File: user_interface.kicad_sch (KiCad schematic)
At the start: 26 parts, among them J1201 PH1-08-UA, J1202 EMI shield frame, J1203 FH12A-40S-0.5SH(55), U1201 TCA9554PW, U1202 AP5725FDCG-7, X1201 Keypad 3x4, X1202 NHD-4.3-480272EF-ASXP

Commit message: Refactor text with ChatGPT and make schematics more readable
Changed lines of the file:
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@@
 		)
 	)
-	(text_box "The graphical interface is a TFT LCD with a backlight.\n\nTouchscreen functionality is provided via the I2C interface.\nThe pins can be disconnected if a non-touchscreen TFT LCD is used."
+	(text_box "The graphical interface consists of a TFT LCD with backlighting.\n- Touchscreen functionality: Provided via the I²C interface.\n- Optional configuration: The I²C pins can be disconnected if a non-touchscreen TFT LCD is used."
 		(exclude_from_sim no)
 		(at 210.82 63.5 0)
@@
 		)
 	)
-	(text_box "They keypad interface is for a 3/4x4 matrix membrane keypad.\n\nThe keypad buttons are polled continuously and button presses are detected by switching rows and columns HIGH/LOW and changing states between INPUT/OUTPUT.\n\nThe keypad buttons and their usage is application defined and thus not hard-set."
+	(text_box "The keypad interface supports a 3×4 or 4×4 matrix membrane keypad.\n- Button scanning: Key presses are detected by continuously polling the keypad and toggling rows and columns between HIGH/LOW and INPUT/OUTPUT states.\n- Application-defined mapping: The functionality and usage of individual keypad buttons are defined by the application and are not fixed."
 		(exclude_from_sim no)
 		(at 13.97 63.5 0)

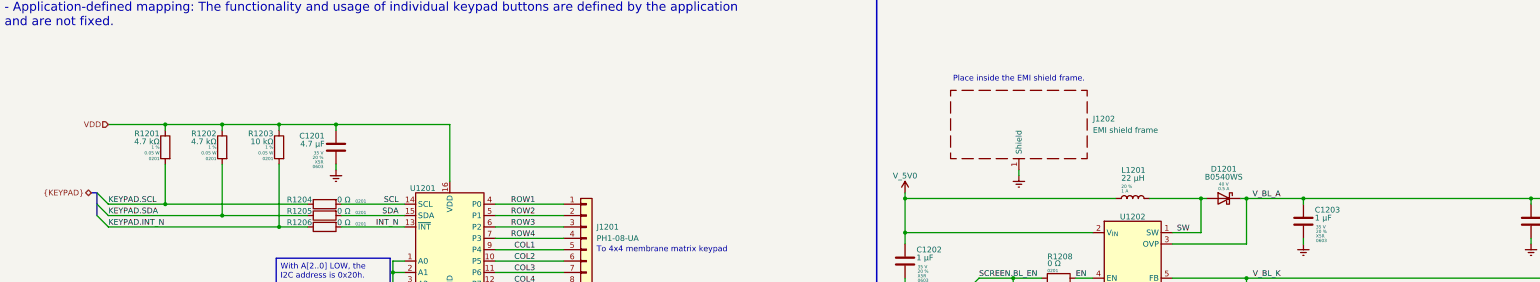
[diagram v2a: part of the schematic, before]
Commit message: Fix power connections
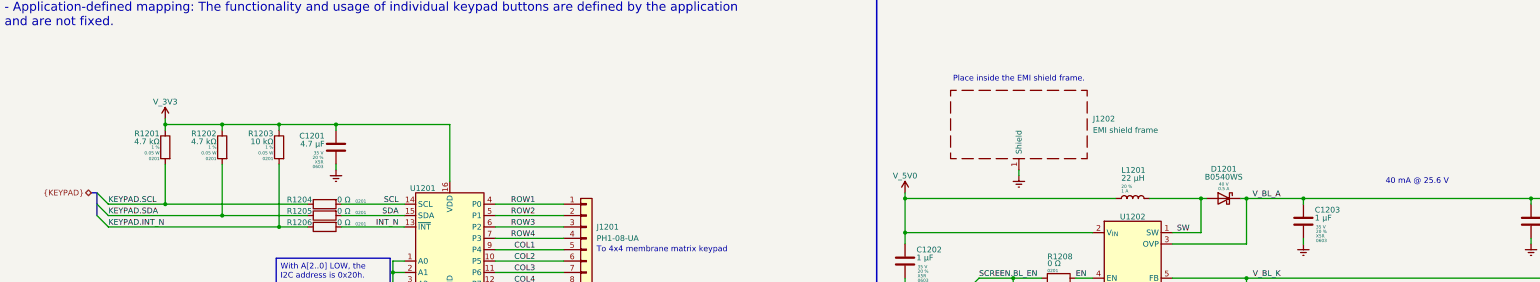
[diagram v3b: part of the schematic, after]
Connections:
- net VDD is gone; now on net V_3V3: C1201.1, R1201.1, R1202.1, R1203.1, U1201.16 (VDD)
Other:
- note added: "40 mA @ 25.6 V"
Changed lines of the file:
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@@
 		)
 	)
+	(text "40 mA @ 25.6 V"
+		(exclude_from_sim no)
+		(at 330.2 114.3 0)
+		(effects
+			(font
+				(size 1.27 1.27)
+			)
+		)
+	)
 	(text "Notes"
 		(exclude_from_sim no)
@@
 	)
 	(junction
-		(at 328.93 143.51)
-		(diameter 0)
-		(color 0 0 0 0)
-	)
-	(junction
 		(at 354.33 227.33)
 		(diameter 0)
@@
 	)
 	(junction
-		(at 50.8 101.6)
-		(diameter 0)
-		(color 0 0 0 0)
-	)
-	(junction
 		(at 354.33 246.38)
 		(diameter 0)
@@
 	)
 	(junction
+		(at 50.8 101.6)
+		(diameter 0)
+		(color 0 0 0 0)
+	)
+	(junction
 		(at 114.3 143.51)
 		(diameter 0)
@@
 	)
 	(junction
+		(at 328.93 143.51)
+		(diameter 0)
+		(color 0 0 0 0)
+	)
+	(junction
 		(at 304.8 118.11)
 		(diameter 0)
@@
 	(wire
 		(pts
-			(xy 38.1 101.6) (xy 50.8 101.6)
+			(xy 90.17 124.46) (xy 104.14 124.46)
 		)
 		(stroke
@@
 		)
 	)
-	(wire
+	(bus
 		(pts
-			(xy 90.17 124.46) (xy 104.14 124.46)
+			(xy 311.15 173.99) (xy 311.15 176.53)
 		)
 		(stroke
@@
 	(bus
 		(pts
-			(xy 311.15 173.99) (xy 311.15 176.53)
+			(xy 311.15 217.17) (xy 311.15 224.79)
 		)
 		(stroke
@@
 		)
 	)
-	(bus
+	(wire
 		(pts
-			(xy 311.15 217.17) (xy 311.15 224.79)
+			(xy 281.94 118.11) (xy 283.21 118.11)
 		)
 		(stroke
@@
 	(wire
 		(pts
-			(xy 281.94 118.11) (xy 283.21 118.11)
+			(xy 365.76 246.38) (xy 368.3 246.38)
 		)
 		(stroke
@@
 	(wire
 		(pts
-			(xy 365.76 246.38) (xy 368.3 246.38)
+			(xy 50.8 100.33) (xy 50.8 101.6)
 		)
 		(stroke
@@
 	(wire
 		(pts
+			(xy 328.93 142.24) (xy 328.93 143.51)
+		)
+		(stroke
+			(width 0)
+			(type default)
+		)
+	)
+	(wire
+		(pts
 			(xy 292.1 135.89) (xy 292.1 144.78)
 		)
@@
 		)
 	)
-	(wire
-		(pts
-			(xy 328.93 142.24) (xy 328.93 143.51)
-		)
-		(stroke
-			(width 0)
-			(type default)
-		)
-	)
 	(bus
 		(pts
@@
 		)
 	)
-	(hierarchical_label "VDD"
-		(shape input)
-		(at 38.1 101.6 180)
-		(effects
-			(font
-				(size 1.27 1.27)
-			)
-			(justify right)
-		)
-	)
 	(hierarchical_label "{SCREEN}"
 		(shape bidirectional)
@@
 		(dnp no)
 		(fields_autoplaced yes)
-		(property "Reference" "#PWR01209"
+		(property "Reference" "#PWR01210"
 			(at 374.65 254 0)
 			(effects
@@
 			(project "linux-sbc"
 				(path "/fa11a02f-8043-4153-ab69-88d766503017/530a7454-1232-4a53-8117-19eb81379b71"
-					(reference "#PWR01209")
+					(reference "#PWR01210")
 					(unit 1)
 				)
@@
 		(dnp no)
 		(fields_autoplaced yes)
-		(property "Reference" "#PWR01201"
+		(property "Reference" "#PWR01202"
 			(at 88.9 118.11 0)
 			(effects
@@
 			(project "linux-sbc"
 				(path "/fa11a02f-8043-4153-ab69-88d766503017/530a7454-1232-4a53-8117-19eb81379b71"
-					(reference "#PWR01201")
+					(reference "#PWR01202")
 					(unit 1)
 				)
@@
 		(dnp no)
 		(fields_autoplaced yes)
-		(property "Reference" "#PWR01202"
+		(property "Reference" "#PWR01203"
 			(at 114.3 151.13 0)
 			(effects
@@
 			(project "linux-sbc"
 				(path "/fa11a02f-8043-4153-ab69-88d766503017/530a7454-1232-4a53-8117-19eb81379b71"
-					(reference "#PWR01202")
+					(reference "#PWR01203")
 					(unit 1)
 				)
@@
 		(on_board yes)
 		(dnp no)
-		(property "Reference" "#PWR01203"
+		(property "Reference" "#PWR01204"
 			(at 215.9 120.65 0)
 			(effects
@@
 			(project "linux-sbc"
 				(path "/fa11a02f-8043-4153-ab69-88d766503017/530a7454-1232-4a53-8117-19eb81379b71"
-					(reference "#PWR01203")
+					(reference "#PWR01204")
 					(unit 1)
 				)
@@
 		(dnp no)
 		(fields_autoplaced yes)
-		(property "Reference" "#PWR01204"
+		(property "Reference" "#PWR01205"
 			(at 215.9 161.29 0)
 			(effects
@@
 			(project "linux-sbc"
 				(path "/fa11a02f-8043-4153-ab69-88d766503017/530a7454-1232-4a53-8117-19eb81379b71"
-					(reference "#PWR01204")
+					(reference "#PWR01205")
 					(unit 1)
 				)
@@
 		(dnp no)
 		(fields_autoplaced yes)
-		(property "Reference" "#PWR01206"
+		(property "Reference" "#PWR01207"
 			(at 304.8 134.62 0)
 			(effects
@@
 			(project "linux-sbc"
 				(path "/fa11a02f-8043-4153-ab69-88d766503017/530a7454-1232-4a53-8117-19eb81379b71"
-					(reference "#PWR01206")
+					(reference "#PWR01207")
 					(unit 1)
 				)
@@
 		(dnp no)
 		(fields_autoplaced yes)
-		(property "Reference" "#PWR01205"
+		(property "Reference" "#PWR01206"
 			(at 241.3 119.38 0)
 			(effects
@@
 			(project "linux-sbc"
 				(path "/fa11a02f-8043-4153-ab69-88d766503017/530a7454-1232-4a53-8117-19eb81379b71"
-					(reference "#PWR01205")
+					(reference "#PWR01206")
 					(unit 1)
 				)
@@
 		(dnp no)
 		(fields_autoplaced yes)
-		(property "Reference" "#PWR01208"
+		(property "Reference" "#PWR01209"
 			(at 355.6 134.62 0)
 			(effects
@@
 			(project "linux-sbc"
 				(path "/fa11a02f-8043-4153-ab69-88d766503017/530a7454-1232-4a53-8117-19eb81379b71"
-					(reference "#PWR01208")
+					(reference "#PWR01209")
 					(unit 1)
 				)
@@
 	)
 	(symbol
+		(lib_id "power:VCC")
+		(at 328.93 142.24 0)
+		(unit 1)
+		(exclude_from_sim no)
+		(in_bom yes)
+		(on_board yes)
+		(dnp no)
+		(property "Reference" "#PWR01208"
+			(at 328.93 146.05 0)
+			(effects
+				(font
+					(size 1.27 1.27)
+				)
+				(hide yes)
+			)
+		)
+		(property "Value" "V_3V3"
+			(at 328.93 139.192 0)
+			(effects
+				(font
+					(size 1.27 1.27)
+				)
+				(justify bottom)
+			)
+		)
+		(property "Footprint" ""
+			(at 328.93 142.24 0)
+			(effects
+				(font
+					(size 1.27 1.27)
+				)
+				(hide yes)
+			)
+		)
+		(property "Datasheet" ""
+			(at 328.93 142.24 0)
+			(effects
+				(font
+					(size 1.27 1.27)
+				)
+				(hide yes)
+			)
+		)
+		(property "Description" "Power symbol creates a global label with name \"VCC\""
+			(at 328.93 142.24 0)
+			(effects
+				(font
+					(size 1.27 1.27)
+				)
+				(hide yes)
+			)
+		)
+		(pin "1"
+		)
+		(instances
+			(project "linux-sbc"
+				(path "/fa11a02f-8043-4153-ab69-88d766503017/530a7454-1232-4a53-8117-19eb81379b71"
+					(reference "#PWR01208")
+					(unit 1)
+				)
+			)
+		)
+	)
+	(symbol
 		(lib_id "Device:C")
 		(at 328.93 240.03 0)
@@
 	)
 	(symbol
-		(lib_id "power:VCC")
-		(at 328.93 142.24 0)
-		(unit 1)
-		(exclude_from_sim no)
-		(in_bom yes)
-		(on_board yes)
-		(dnp no)
-		(property "Reference" "#PWR01207"
-			(at 328.93 146.05 0)
-			(effects
-				(font
-					(size 1.27 1.27)
-				)
-				(hide yes)
-			)
-		)
-		(property "Value" "V_3V3"
-			(at 328.93 139.192 0)
-			(effects
-				(font
-					(size 1.27 1.27)
-				)
-				(justify bottom)
-			)
-		)
-		(property "Footprint" ""
-			(at 328.93 142.24 0)
-			(effects
-				(font
-					(size 1.27 1.27)
-				)
-				(hide yes)
-			)
-		)
-		(property "Datasheet" ""
-			(at 328.93 142.24 0)
-			(effects
-				(font
-					(size 1.27 1.27)
-				)
-				(hide yes)
-			)
-		)
-		(property "Description" "Power symbol creates a global label with name \"VCC\""
-			(at 328.93 142.24 0)
-			(effects
-				(font
-					(size 1.27 1.27)
-				)
-				(hide yes)
-			)
-		)
-		(pin "1"
-		)
-		(instances
-			(project "linux-sbc"
-				(path "/fa11a02f-8043-4153-ab69-88d766503017/530a7454-1232-4a53-8117-19eb81379b71"
-					(reference "#PWR01207")
-					(unit 1)
-				)
-			)
-		)
-	)
-	(symbol
 		(lib_id "Device:R")
 		(at 63.5 106.68 0)
@@
 					(unit 1)
 				)
+			)
+		)
+	)
+	(symbol
+		(lib_id "power:VCC")
+		(at 50.8 100.33 0)
+		(unit 1)
+		(exclude_from_sim no)
+		(in_bom yes)
+		(on_board yes)
+		(dnp no)
+		(property "Reference" "#PWR01201"
+			(at 50.8 104.14 0)
+			(effects
+				(font
+					(size 1.27 1.27)
+				)
+				(hide yes)
+			)
+		)
+		(property "Value" "V_3V3"
+			(at 50.8 97.282 0)
+			(effects
+				(font
+					(size 1.27 1.27)
+				)
+				(justify bottom)
+			)
+		)
+		(property "Footprint" ""
+			(at 50.8 100.33 0)
+			(effects
+				(font
+					(size 1.27 1.27)
+				)
+				(hide yes)
+			)
+		)
+		(property "Datasheet" ""
+			(at 50.8 100.33 0)
+			(effects
+				(font
+					(size 1.27 1.27)
+				)
+				(hide yes)
+			)
+		)
+		(property "Description" "Power symbol creates a global label with name \"VCC\""
+			(at 50.8 100.33 0)
+			(effects
+				(font
+					(size 1.27 1.27)
+				)
+				(hide yes)
+			)
+		)
+		(pin "1"
+		)
+		(instances
+			(project "linux-sbc"
+				(path "/fa11a02f-8043-4153-ab69-88d766503017/530a7454-1232-4a53-8117-19eb81379b71"
+					(reference "#PWR01201")
+					(unit 1)
+				)

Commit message: Clean up schematics
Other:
- note removed: "To 4x4 membrane matrix keypad"
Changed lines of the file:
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@@
 	(title_block
 		(title "Linux SBC")
-		(date "2025-12-19")
+		(date "2025-12-26")
 		(rev "v1.0.0")
 	)
@@
 		)
 	)
-	(text "To 4x4 membrane matrix keypad"
-		(exclude_from_sim no)
-		(at 147.066 129.5401 0)
-		(effects
-			(font
-				(size 1.27 1.27)
-			)
-			(justify left)
-		)
-	)
 	(text "Place inside the EMI shield frame."
 		(exclude_from_sim no)
@@
 	)
 	(junction
-		(at 101.6 134.62)
-		(diameter 0)
-		(color 0 0 0 0)
-	)
-	(junction
 		(at 368.3 224.79)
 		(diameter 0)
@@
 	)
 	(junction
-		(at 101.6 137.16)
-		(diameter 0)
-		(color 0 0 0 0)
-	)
-	(junction
 		(at 215.9 125.73)
 		(diameter 0)
@@
 	)
 	(junction
+		(at 102.87 134.62)
+		(diameter 0)
+		(color 0 0 0 0)
+	)
+	(junction
 		(at 215.9 118.11)
 		(diameter 0)
@@
 	)
 	(junction
+		(at 102.87 137.16)
+		(diameter 0)
+		(color 0 0 0 0)
+	)
+	(junction
 		(at 240.03 153.67)
 		(diameter 0)
@@
 	(wire
 		(pts
-			(xy 104.14 132.08) (xy 101.6 132.08)
+			(xy 102.87 132.08) (xy 104.14 132.08)
 		)
 		(stroke
@@
 	(wire
 		(pts
+			(xy 102.87 134.62) (xy 104.14 134.62)
+		)
+		(stroke
+			(width 0)
+			(type default)
+		)
+	)
+	(wire
+		(pts
 			(xy 88.9 101.6) (xy 88.9 102.87)
 		)
@@
 	(wire
 		(pts
-			(xy 101.6 137.16) (xy 101.6 143.51)
+			(xy 102.87 137.16) (xy 102.87 143.51)
 		)
 		(stroke
@@
 	(wire
 		(pts
+			(xy 102.87 137.16) (xy 104.14 137.16)
+		)
+		(stroke
+			(width 0)
+			(type default)
+		)
+	)
+	(wire
+		(pts
 			(xy 304.8 118.11) (xy 355.6 118.11)
 		)
@@
 	(wire
 		(pts
-			(xy 101.6 132.08) (xy 101.6 134.62)
+			(xy 102.87 132.08) (xy 102.87 134.62)
 		)
 		(stroke
@@
 	(wire
 		(pts
-			(xy 101.6 134.62) (xy 101.6 137.16)
+			(xy 102.87 134.62) (xy 102.87 137.16)
 		)
 		(stroke
@@
 	(wire
 		(pts
-			(xy 114.3 143.51) (xy 101.6 143.51)
+			(xy 114.3 143.51) (xy 102.87 143.51)
 		)
 		(stroke
@@
 	(wire
 		(pts
-			(xy 101.6 134.62) (xy 104.14 134.62)
-		)
-		(stroke
-			(width 0)
-			(type default)
-		)
-	)
-	(wire
-		(pts
 			(xy 313.69 199.39) (xy 369.57 199.39)
 		)
@@
 	(wire
 		(pts
-			(xy 101.6 137.16) (xy 104.14 137.16)
-		)
-		(stroke
-			(width 0)
-			(type default)
-		)
-	)
-	(wire
-		(pts
 			(xy 275.59 143.51) (xy 276.86 143.51)
 		)
@@
 		(dnp no)
 		(property "Reference" "J1201"
-			(at 147.066 124.46 0)
+			(at 147.32 125.73 0)
 			(effects
 				(font
@@
 		)
 		(property "Value" "PH1-08-UA"
-			(at 147.066 127 0)
+			(at 147.32 128.27 0)
 			(effects
 				(font
@@
 		(on_board yes)
 		(dnp no)
-		(fields_autoplaced yes)
 		(property "Reference" "J1203"
-			(at 377.19 184.5055 0)
+			(at 377.19 182.88 0)
 			(effects
 				(font
@@
 		)
 		(property "Value" "FH12A-40S-0.5SH(55)"
-			(at 377.19 187.0455 0)
+			(at 377.19 185.42 0)
 			(effects
 				(font

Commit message: Layout the UI section
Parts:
- added R1210, R1211, R1212, R1213, R1214, R1215, R1216, R1217, R1218, R1219, R1220, R1221, R1222, R1223, R1224, R1225, R1226, R1227, R1228, R1229, R1230, R1231, R1232, R1233, R1234, R1235, R1236, R1237, R1238, R1239, R1240, R1241, R1242: 0 Ω, perfect_footprints:R_0201_0603Metric, symbol Device:R
- C1205: footprint Capacitor_SMD:C_0603_1608Metric -> perfect_footprints:C_0402_1005Metric; Digi-Key Part Number 490-7205-1-ND -> 1276-6836-1-ND; MPN GRM188R6YA475KE15D -> CL05A475MO5NUNC; Manufacturer Murata Electronics -> Samsung Electro-Mechanics; Size 0603 -> 0402; Voltage rating 35 V -> 16 V
- J1202: footprint RF_Shielding:Laird_Technologies_BMI-S-203-F_26.21x26.21mm -> RF_Shielding:Laird_Technologies_BMI-S-202-F_16.50x16.50mm
- renumbered R1208 to R1207, R1207 to R1208, R1210 to R1243, R1211 to R1244
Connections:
- net EN: now also R1208.1
- net SCL: now also J1203.39 (Pin_39), R1241.2
- net SCREEN.B0: now also R1226.1; no longer J1203.21 (Pin_21)
- net SCREEN.B1: now also R1227.1; no longer J1203.22 (Pin_22)
- net SCREEN.B2: now also R1228.1; no longer J1203.23 (Pin_23)
- net SCREEN.B3: now also R1229.1; no longer J1203.24 (Pin_24)
- net SCREEN.B4: now also R1230.1; no longer J1203.25 (Pin_25)
- net SCREEN.B5: now also R1231.1; no longer J1203.26 (Pin_26)
- net SCREEN.B6: now also R1232.1; no longer J1203.27 (Pin_27)
- net SCREEN.B7: now also R1233.1; no longer J1203.28 (Pin_28)
- net SCREEN.BL_EN: no longer R1208.1
- net SCREEN.DCLK: now also R1234.1; no longer J1203.30 (Pin_30)
- net SCREEN.DE: now also R1238.1; no longer J1203.34 (Pin_34)
- net SCREEN.DISP: now also R1235.1; no longer J1203.31 (Pin_31), R1244.1
- net SCREEN.G0: now also R1218.1; no longer J1203.13 (Pin_13)
- net SCREEN.G1: now also R1219.1; no longer J1203.14 (Pin_14)
- net SCREEN.G2: now also R1220.1; no longer J1203.15 (Pin_15)
- net SCREEN.G3: now also R1221.1; no longer J1203.16 (Pin_16)
- net SCREEN.G4: now also R1222.1; no longer J1203.17 (Pin_17)
- net SCREEN.G5: now also R1223.1; no longer J1203.18 (Pin_18)
- net SCREEN.G6: now also R1224.1; no longer J1203.19 (Pin_19)
- net SCREEN.G7: now also R1225.1; no longer J1203.20 (Pin_20)
- net SCREEN.HSYNC: now also R1236.1; no longer J1203.32 (Pin_32)
- net SCREEN.INT: now also R1240.1; no longer J1203.38 (Pin_38)
- net SCREEN.R0: now also R1210.1; no longer J1203.5 (Pin_5)
- net SCREEN.R1: now also R1211.1; no longer J1203.6 (Pin_6)
- net SCREEN.R2: now also R1212.1; no longer J1203.7 (Pin_7)
- net SCREEN.R3: now also R1213.1; no longer J1203.8 (Pin_8)
- net SCREEN.R4: now also R1214.1; no longer J1203.9 (Pin_9)
- net SCREEN.R5: now also R1215.1; no longer J1203.10 (Pin_10)
- net SCREEN.R6: now also R1216.1; no longer J1203.11 (Pin_11)
- net SCREEN.R7: now also R1217.1; no longer J1203.12 (Pin_12)
- net SCREEN.RST: now also R1239.1; no longer J1203.37 (Pin_37), R1243.1
- net SCREEN.SCL: now also R1241.1; no longer J1203.39 (Pin_39)
- net SCREEN.SDA: now also R1242.1; no longer J1203.40 (Pin_40)
- net SCREEN.VSYNC: now also R1237.1; no longer J1203.33 (Pin_33)
- net SDA: now also J1203.40 (Pin_40), R1242.2
- new net B0: J1203.21 (Pin_21), R1226.2
- new net B1: J1203.22 (Pin_22), R1227.2
- new net B2: J1203.23 (Pin_23), R1228.2
- new net B3: J1203.24 (Pin_24), R1229.2
- new net B4: J1203.25 (Pin_25), R1230.2
- new net B5: J1203.26 (Pin_26), R1231.2
- new net B6: J1203.27 (Pin_27), R1232.2
- new net B7: J1203.28 (Pin_28), R1233.2
- new net DCLK: J1203.30 (Pin_30), R1234.2
- new net DE: J1203.34 (Pin_34), R1238.2
- new net DISP: J1203.31 (Pin_31), R1235.2, R1244.1
- new net G0: J1203.13 (Pin_13), R1218.2
- new net G1: J1203.14 (Pin_14), R1219.2
- new net G2: J1203.15 (Pin_15), R1220.2
- new net G3: J1203.16 (Pin_16), R1221.2
- new net G4: J1203.17 (Pin_17), R1222.2
- new net G5: J1203.18 (Pin_18), R1223.2
- new net G6: J1203.19 (Pin_19), R1224.2
- new net G7: J1203.20 (Pin_20), R1225.2
- new net HSYNC: J1203.32 (Pin_32), R1236.2
- new net INT: J1203.38 (Pin_38), R1240.2
- new net R0: J1203.5 (Pin_5), R1210.2
- new net R1: J1203.6 (Pin_6), R1211.2
- new net R2: J1203.7 (Pin_7), R1212.2
- new net R3: J1203.8 (Pin_8), R1213.2
- new net R4: J1203.9 (Pin_9), R1214.2
- new net R5: J1203.10 (Pin_10), R1215.2
- new net R6: J1203.11 (Pin_11), R1216.2
- new net R7: J1203.12 (Pin_12), R1217.2
- new net RST: J1203.37 (Pin_37), R1239.2, R1243.1
- new net VSYNC: J1203.33 (Pin_33), R1237.2
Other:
- moved on the sheet: C1202, C1203, C1204, C1206, D1201, J1202, J1203, L1201, R1207, R1208, R1209, R1243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

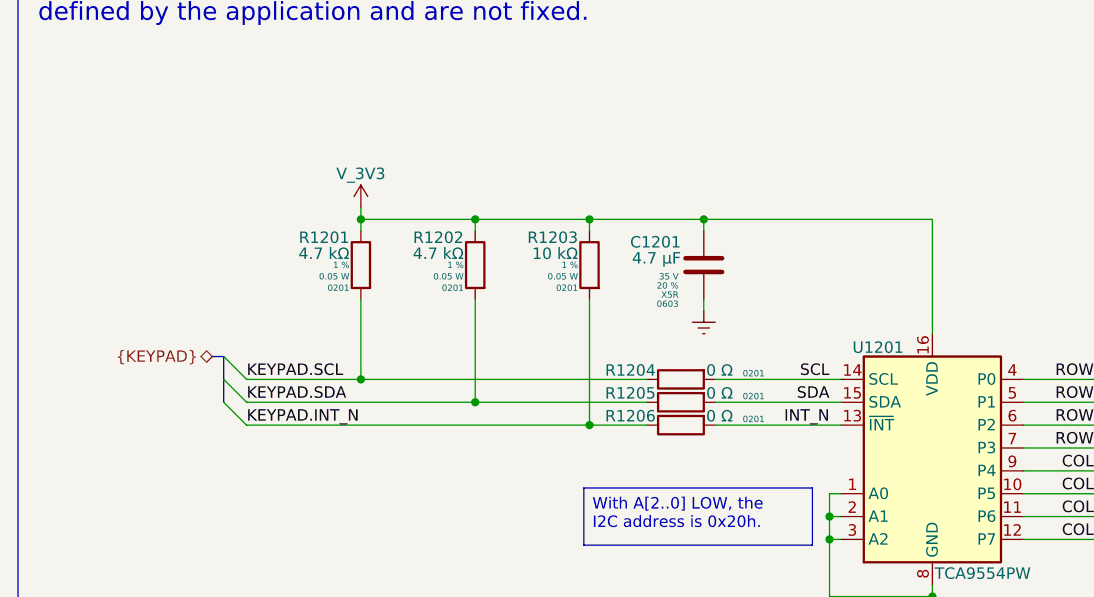
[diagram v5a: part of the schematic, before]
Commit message: Remove redundant test points, fix layouts
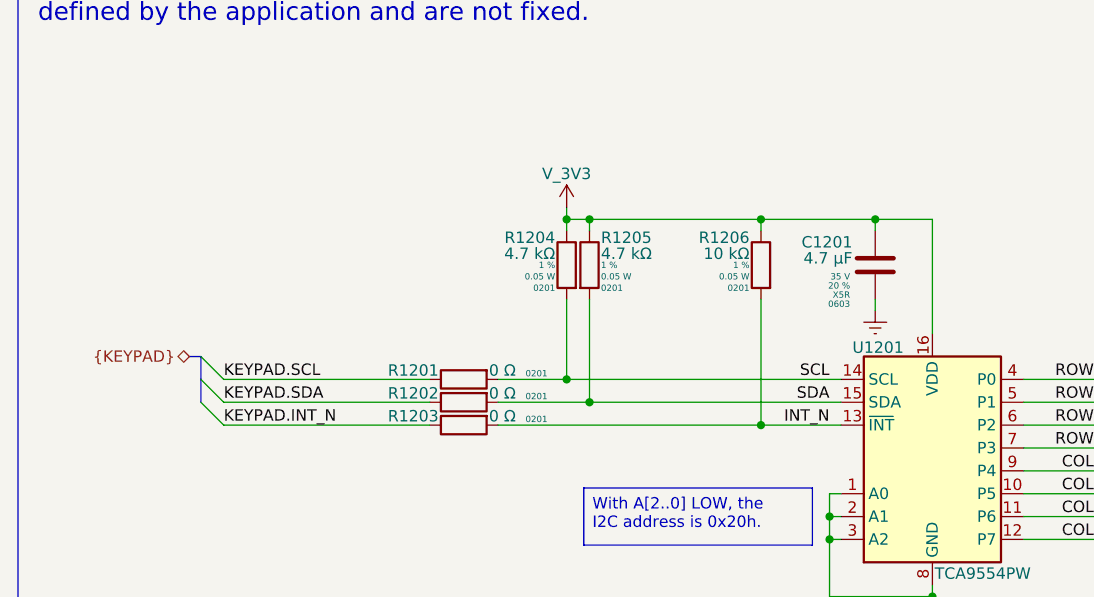
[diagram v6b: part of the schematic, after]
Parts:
- renumbered R1204 to R1201, R1205 to R1202, R1206 to R1203, R1201 to R1204, R1202 to R1205, R1203 to R1206
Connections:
- net INT_N: now also R1206.2
- net KEYPAD.INT_N: no longer R1206.2
- net KEYPAD.SCL: no longer R1204.2
- net KEYPAD.SDA: no longer R1205.2
- net SCL: now also R1204.2
- net SDA: now also R1205.2
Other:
- moved on the sheet: C1201, R1201, R1202, R1203, R1204, R1205, R1206
